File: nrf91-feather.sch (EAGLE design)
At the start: 87 parts, among them J2 CON-HEADER-1X12-MALE-PIN, J3 CON-HEADER-1X16-MALE-PIN, J4 CON-1909763-1, J5 CON-SIM-104224-0820, J6 CON-S2B-PH-SM4-TB(LF)(SN), J7 CON-1909763-1, J8 CON-USB-DX07S016JA1R1500, J9 CON-TC2030-MCP-NL, Q2 MOSFET-DUAL-COMP-SOT563, Q3 MOSFET-P-20V-4.7A-SOT23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

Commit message: V5 Proto 1
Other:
- note added: "TODO: investigate what GPIOs are necesary"
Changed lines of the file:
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@@
 <text x="134.62" y="15.24" size="3.81" layer="97">Some footprints provided by SnapEDA</text>
 <text x="134.62" y="10.16" size="3.81" layer="97">Some schematic symbols from Sparkfun</text>
+<text x="259.08" y="83.82" size="1.778" layer="91">TODO: investigate what GPIOs are necesary</text>
 </plain>
 <instances>

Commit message: Modifications
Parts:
- removed JMP4: JUMPER-NC, wolff-den:JUMPER-NC
- removed Q5: MOSFET-N-SC89, wolff-den:MOSFET-N-SC89
- removed R7: 1M, wolff-den:RES-1M-5%-0402
- added Q1: MOSFET-N-SC89, wolff-den:MOSFET-N-SC89
- JMP5: value JUMPER-NC -> JUMPER-NO-ROUND-NO; device wolff-den:JUMPER-NC -> wolff-den:JUMPER-NO-ROUND-NO
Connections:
- removed net !EN: J2.2, Q5.G, R19.2
- removed net PS_EN: Q5.D, R5.1, U3.EN
- removed net PS_MODE: JMP4.2, R7.2, U3.MODE
- new net EN: J2.2, R19.2, U3.EN
- new net N$12: Q1.G, R5.2, U2.GPIO.0/CLK
- net !RESET: now also Q1.D; no longer U2.GPIO.0/CLK
- net GND: now also Q1.S, R5.1, U3.MODE; no longer Q5.S, R19.1, R7.1
- net P0.13/A0: no longer JMP4.1
- net VBUS: now also JMP2.1
- net VSYS: now also R19.1; no longer JMP2.1, R5.2
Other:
- moved on the sheet: R19, R5

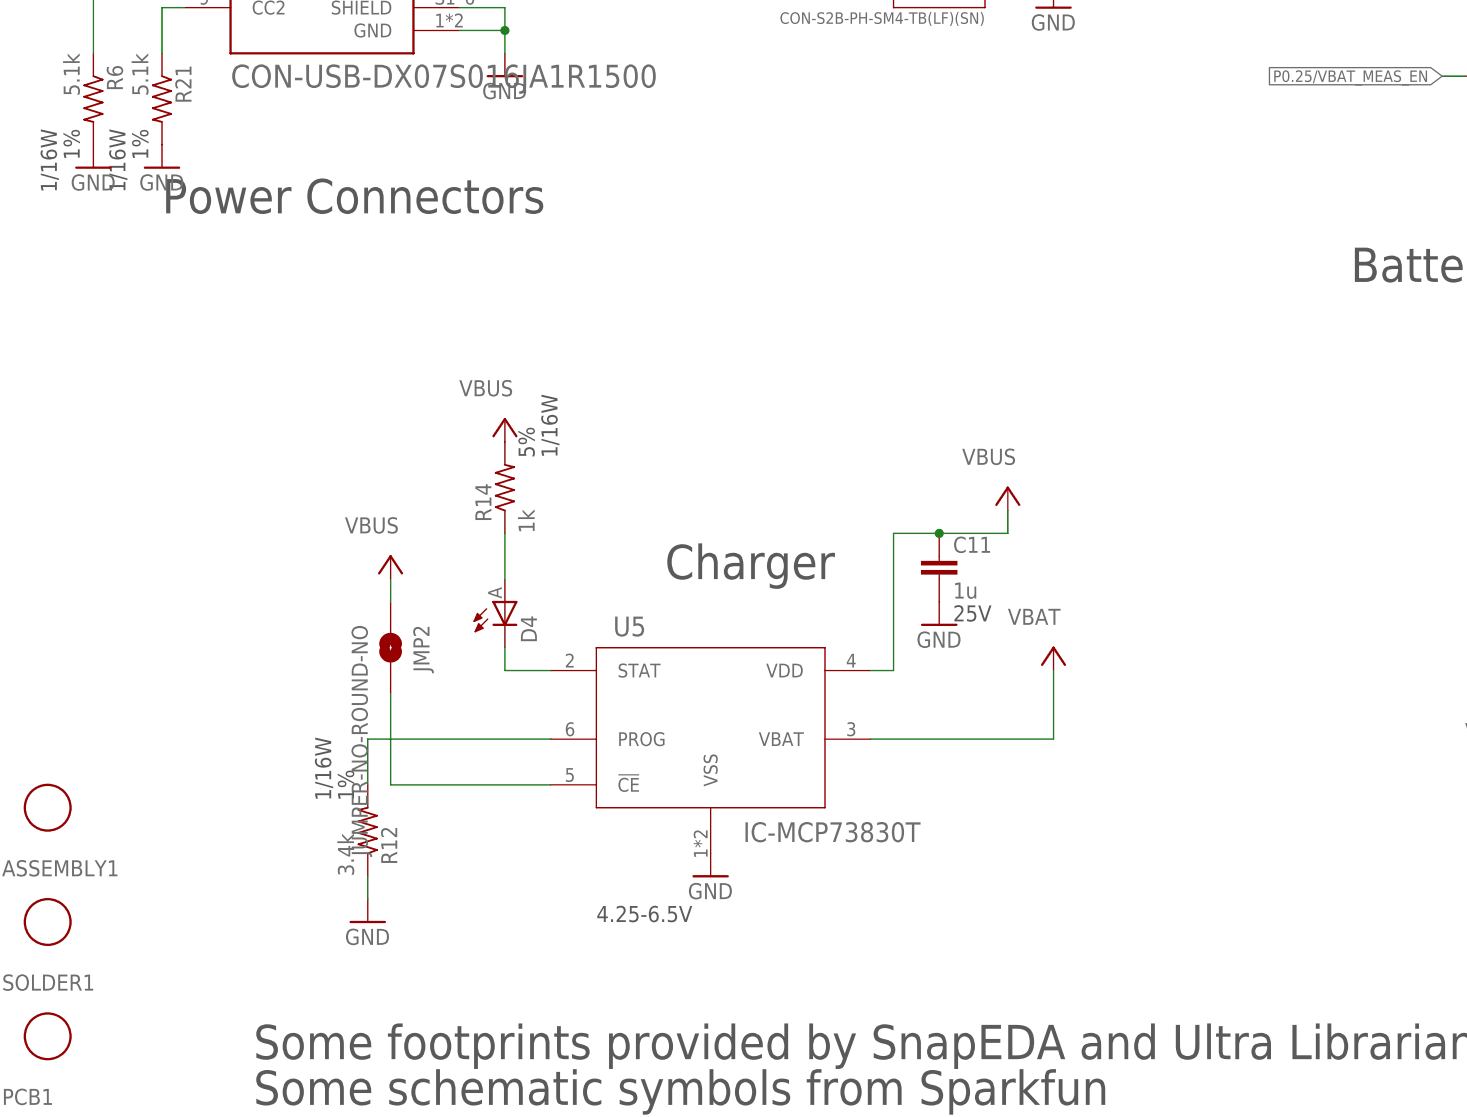
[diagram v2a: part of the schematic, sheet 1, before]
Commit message: Updating use of WP and HOLD pins
Changed
* Removed connections directly to mcu and replaced with pull-ups
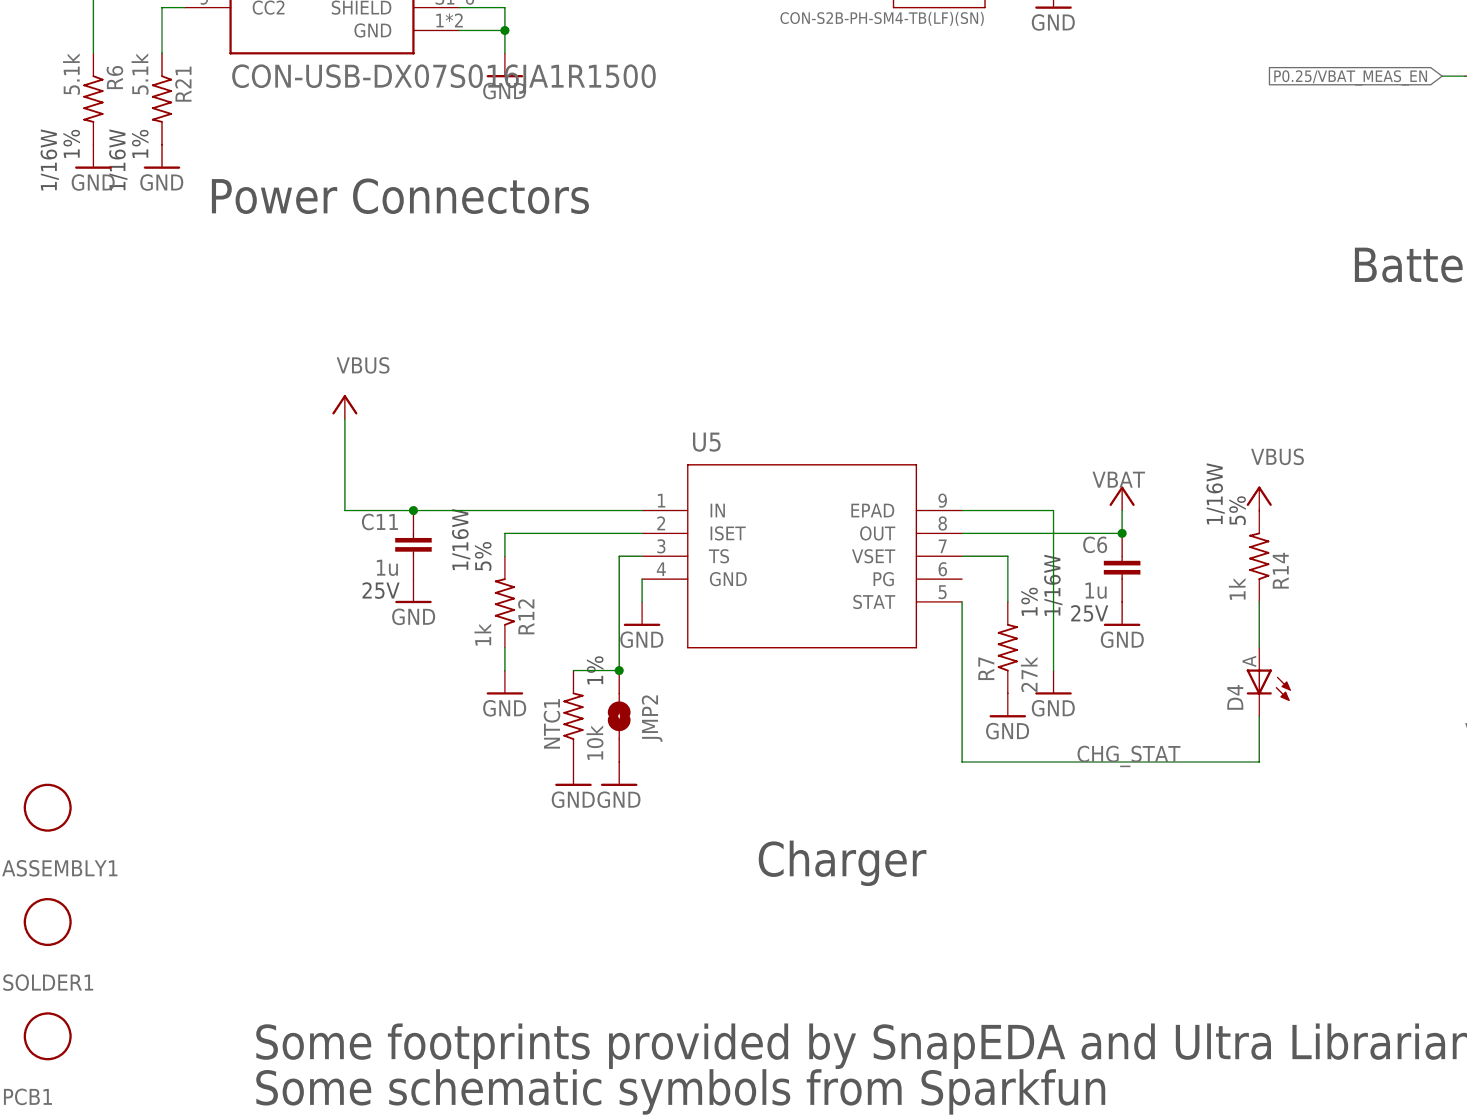
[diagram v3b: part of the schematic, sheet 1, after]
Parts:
- added C6: 1u, wolff-den:CAP-1U-25V-1-0402
- added NTC1: 10k, wolff-den:NTC-10K-1%-0402
- added R22, R23: 100k, wolff-den:RES-100K-1%-0402
- added R7: 27k, wolff-den:RES-27K-1%-0402
- R12: value 3.4k -> 1k; device wolff-den:RES-3.4K-1%-0402 -> wolff-den:RES-1K-5%-0402
- R9: value 1M -> 100k; device wolff-den:RES-1M-5%-0402 -> wolff-den:RES-100K-1%-0402
- U4: value POWER-SWITCH-MIC94092YC6 -> POWER-SWITCH-SIP32409-DFN4; device wolff-den:POWER-SWITCH-MIC94092YC6 -> wolff-den:POWER-SWITCH-SIP32409-DFN4
- U5: value IC-MCP73830T -> IC-BQ25170JDSGR-WSON8; device wolff-den:IC-MCP73830T -> wolff-den:IC-BQ25170JDSGR-WSON8
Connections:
- net CHRG renamed CHG_STAT
- removed net FLASH_HOLD: U1.P0.10, U6.!HOLD
- removed net FLASH_WP: U1.P0.08, U6.!WP
- removed net PROG: R12.2, U5.PROG
- new net CHG_ISET: R12.2, U5.ISET
- new net CHG_TS: JMP2.1, NTC1.2, U5.TS
- new net CHG_VSET: R7.2, U5.VSET
- new net N$14: R22.1, U6.!HOLD
- net +3V3: now also R22.2, R23.2
- net GND: now also C6.2, JMP2.2, NTC1.1, R7.1, U5.EPAD, U5.GND; no longer U5.VSS
- net N$9: now also R23.1, U6.!WP; no longer JMP2.2, U5.!CE
- net VBAT: now also C6.1, U5.OUT; no longer U5.VBAT
- net VBUS: now also U5.IN; no longer JMP2.1, U5.VDD
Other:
- note removed: "4.25-6.5V"
- moved on the sheet: C11, D4, JMP2, R12, R14

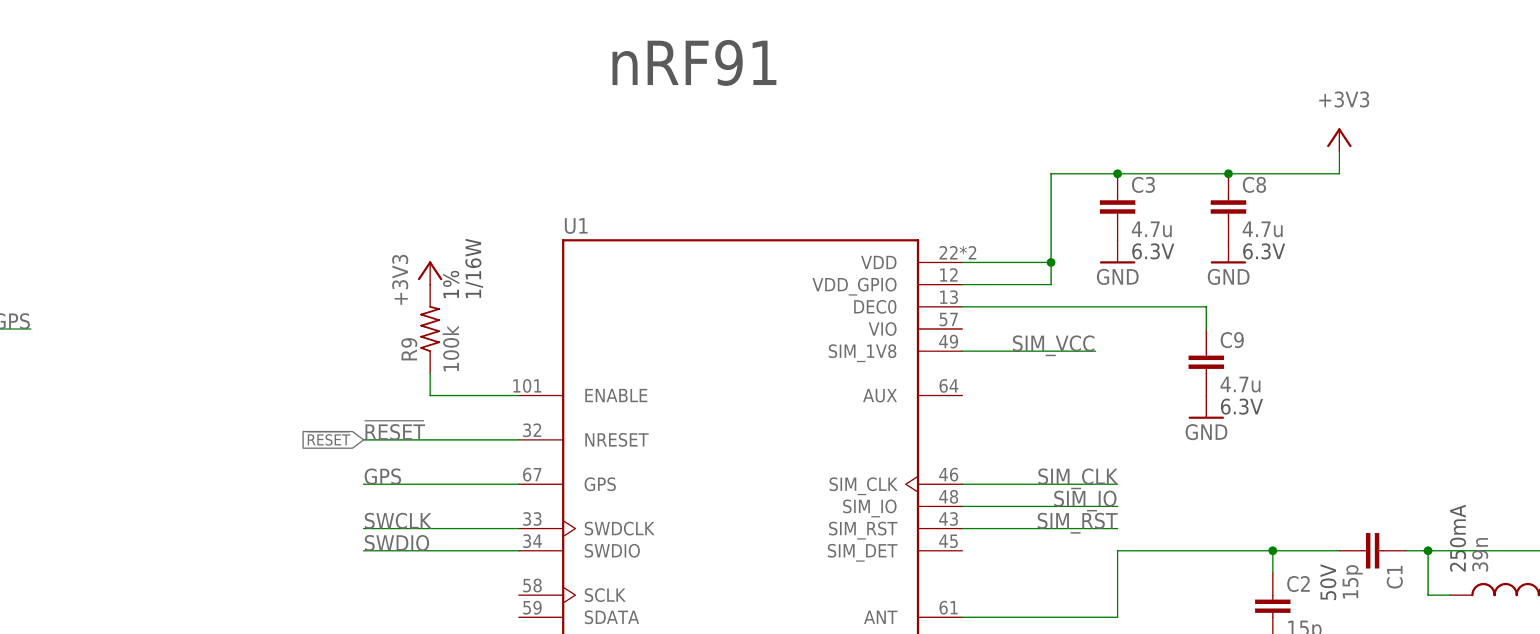
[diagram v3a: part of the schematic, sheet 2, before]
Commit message: Adding updated bypass and filtering for power supply
Changed:
* Ferrite and 47u for power inputs
* Re-routed battery measurement circuit
* Cleaned up
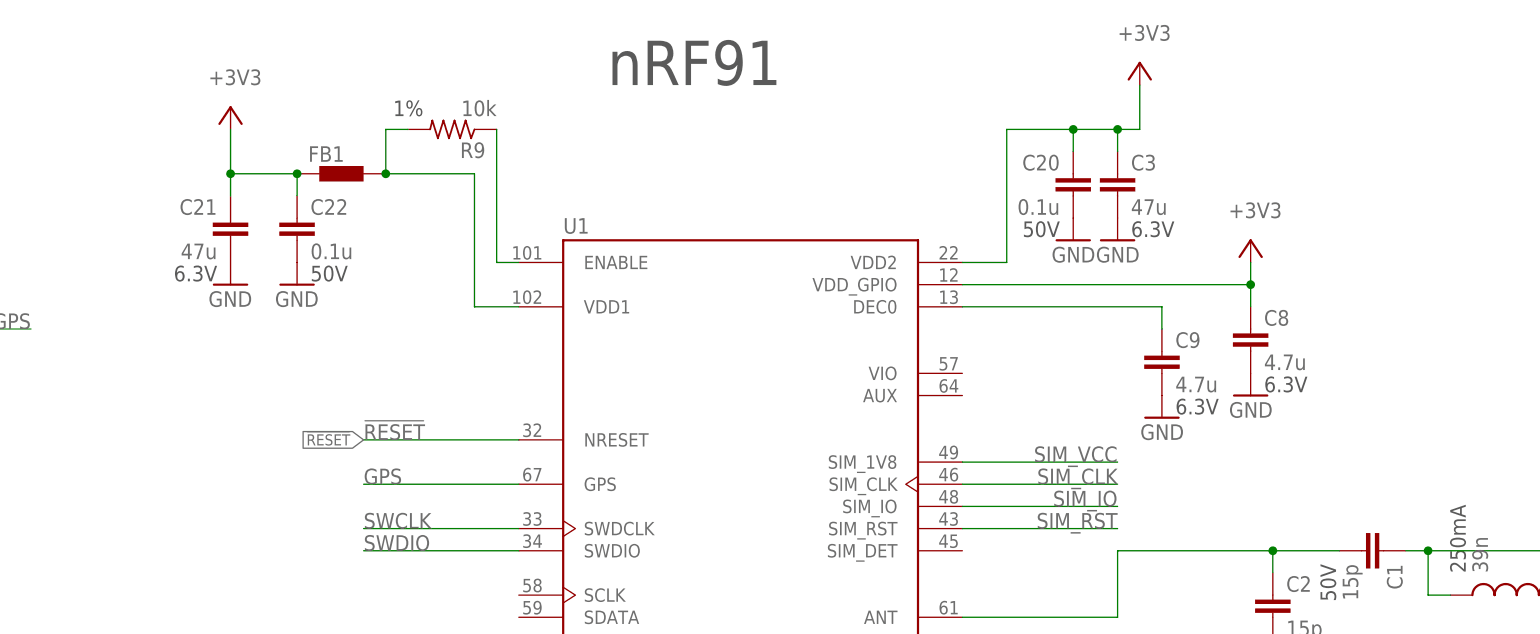
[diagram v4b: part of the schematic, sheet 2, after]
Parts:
- removed Q1: MOSFET-N-SC89, wolff-den:MOSFET-N-SC89
- added C20, C22: 0.1u, wolff-den:CAP-0.1U-50V-0402
- added C21: 47u, wolff-den:CAP-47U-6.3V-0805
- added FB1: FERRITE-120-100MHZ-0402, wolff-den:FERRITE-120-100MHZ-0402
- C3: value 4.7u -> 47u; device wolff-den:CAP-4.7U-6.3V-2-0603 -> wolff-den:CAP-47U-6.3V-0805
- R9: value 100k -> 10k; device wolff-den:RES-100K-1%-0402 -> wolff-den:RES-10K-1%-0402
- renumbered JMP5 to JMP4
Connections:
- removed net N$12: Q1.G, R5.2, U2.GPIO.0/CLK
- new net N$16: FB1.2, R9.2, U1.VDD1
- net !RESET: now also U2.GPIO.0/CLK; no longer Q1.D
- net +3V3: now also C20.1, C21.1, C22.1, FB1.1, U1.VDD2; no longer R9.2, U1.VDD
- net GND: now also C20.2, C21.2, C22.2; no longer Q1.S
- net P0.25/VBAT_MEAS_EN: now also R5.2
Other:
- moved on the sheet: C3, C8, C9, R5, R9
